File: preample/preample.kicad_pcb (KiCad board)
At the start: 4 copper layers, 158 x 37 mm, 74 parts, among them J1 Conn_01x03, J2 Conn_01x07, J3 Conn_01x06, SW1 SW_DPDT_x2, U1 TPS7A39, U2 OPA2134UA, U3 OPA134UA, U4 OPA2134UA, U5 OPA134UA

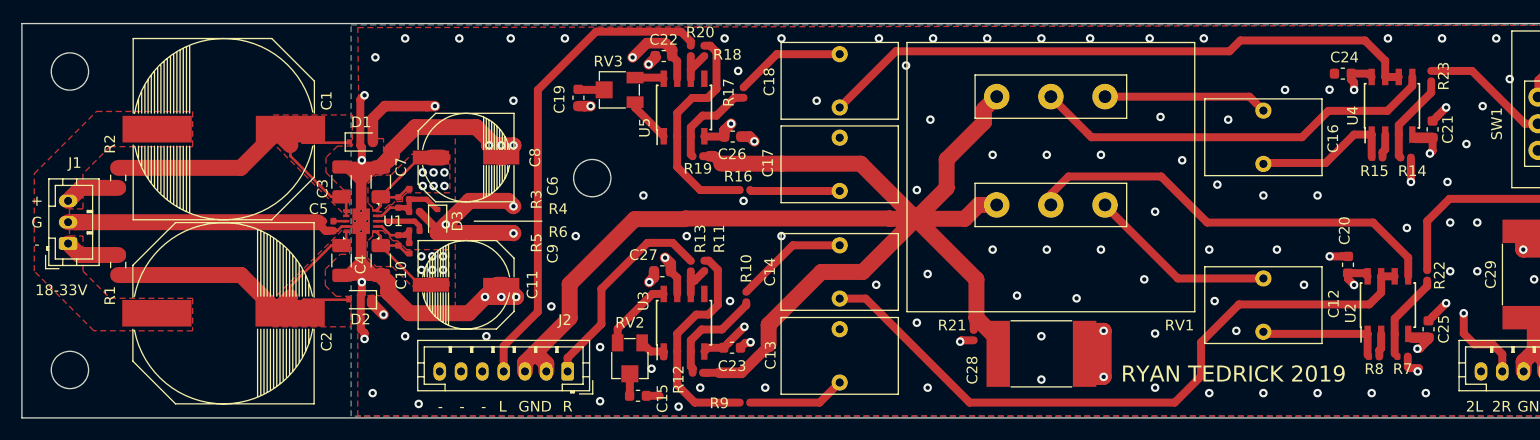
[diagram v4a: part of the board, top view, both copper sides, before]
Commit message: Changes resistors for opamps to 0805s. Chose more realistic power resistors. rerouted for new components.
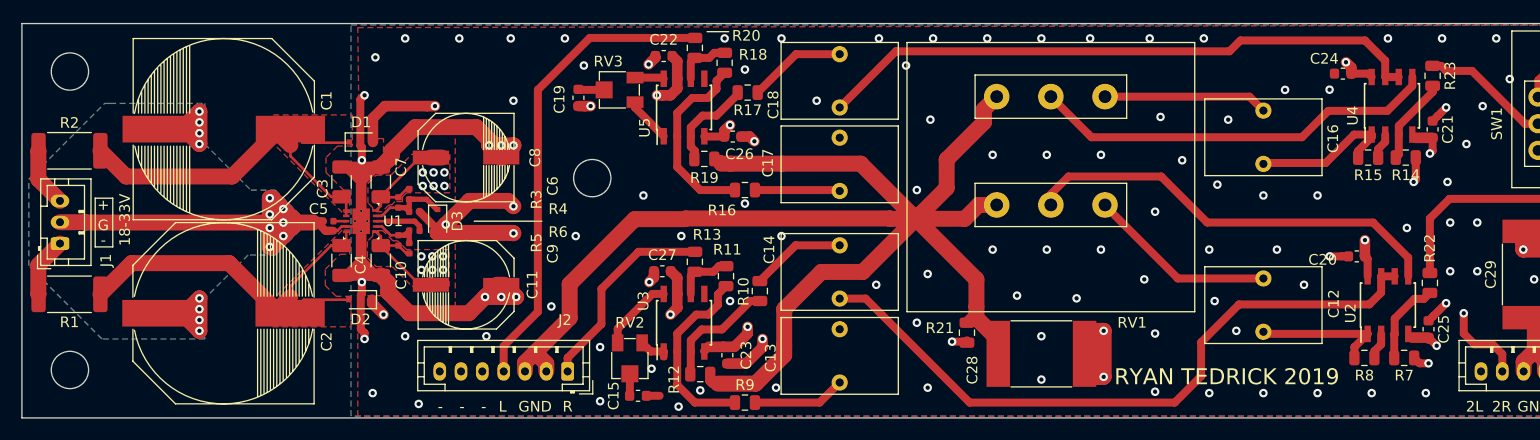
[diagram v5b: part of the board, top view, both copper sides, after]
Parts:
- R1, R2: value 3R -> 15R; footprint Resistor_SMD:R_0805_2012Metric -> Resistor_SMD:R_2512_6332Metric
- R10, R11, R12, R16, R17, R18, R19, R9: value 560R -> 5K6; footprint Resistor_SMD:R_0402_1005Metric -> Resistor_SMD:R_0805_2012Metric
- R13, R14, R15, R20, R21, R22, R23, R7, R8: footprint Resistor_SMD:R_0402_1005Metric -> Resistor_SMD:R_0805_2012Metric
- moved R1 5.33 mm to (50.5, 75.3), turned to 180 degrees
- moved R2 5.23 mm to (50.5, 61.8), turned to 0 degrees
- moved R11 2.25 mm to (112.1, 73.6), turned to 270 degrees
- moved R18 2.21 mm to (112.0, 53.6), turned to 270 degrees
- moved R10 1.39 mm to (115.3, 75.0)
- moved C20 1.14 mm to (171.3, 71.8), turned to 0 degrees
- moved R8 0.92 mm to (172.0, 81.3)
- moved R15 0.86 mm to (172.4, 62.5)
- moved C23 0.83 mm to (112.3, 81.0), turned to 90 degrees
- moved J1 0.76 mm to (49.7, 70.5)
- moved R22 0.76 mm to (178.2, 74.2)
- moved R21 0.67 mm to (134.7, 78.9)
- moved R19 0.66 mm to (110.1, 62.6)
- moved R13 0.56 mm to (109.2, 72.3)
- moved R20 0.47 mm to (109.2, 52.2)
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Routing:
- net GND: track 180.6 -> 222.1 mm, vias 120 -> 138
- net Net-(R16-Pad1): track 21.3 -> 17.8 mm
- net -24V: track 34.2 -> 37.5 mm
- net Net-(R11-Pad2): track 21.2 -> 17.9 mm
- net +24V: track 34.9 -> 37.9 mm
- net SIGNAL_GROUND: track 137.7 -> 140.1 mm
- net -15V: track 202.8 -> 201.0 mm
- net +15V: track 182.8 -> 181.1 mm
- net Net-(C14-Pad1): track 10.6 -> 8.88 mm
- net Net-(R11-Pad1): track 3.77 -> 5.37 mm
- net Net-(R10-Pad2): track 9.97 -> 11.2 mm
- net Net-(R18-Pad1): track 3.92 -> 5.10 mm
- net Net-(C18-Pad1): track 10.3 -> 9.19 mm
- net CH1_OUT: track 19.9 -> 19.3 mm
- net CH2_OUT: track 45.1 -> 44.5 mm
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- added copper zone on In2.Cu, net GND

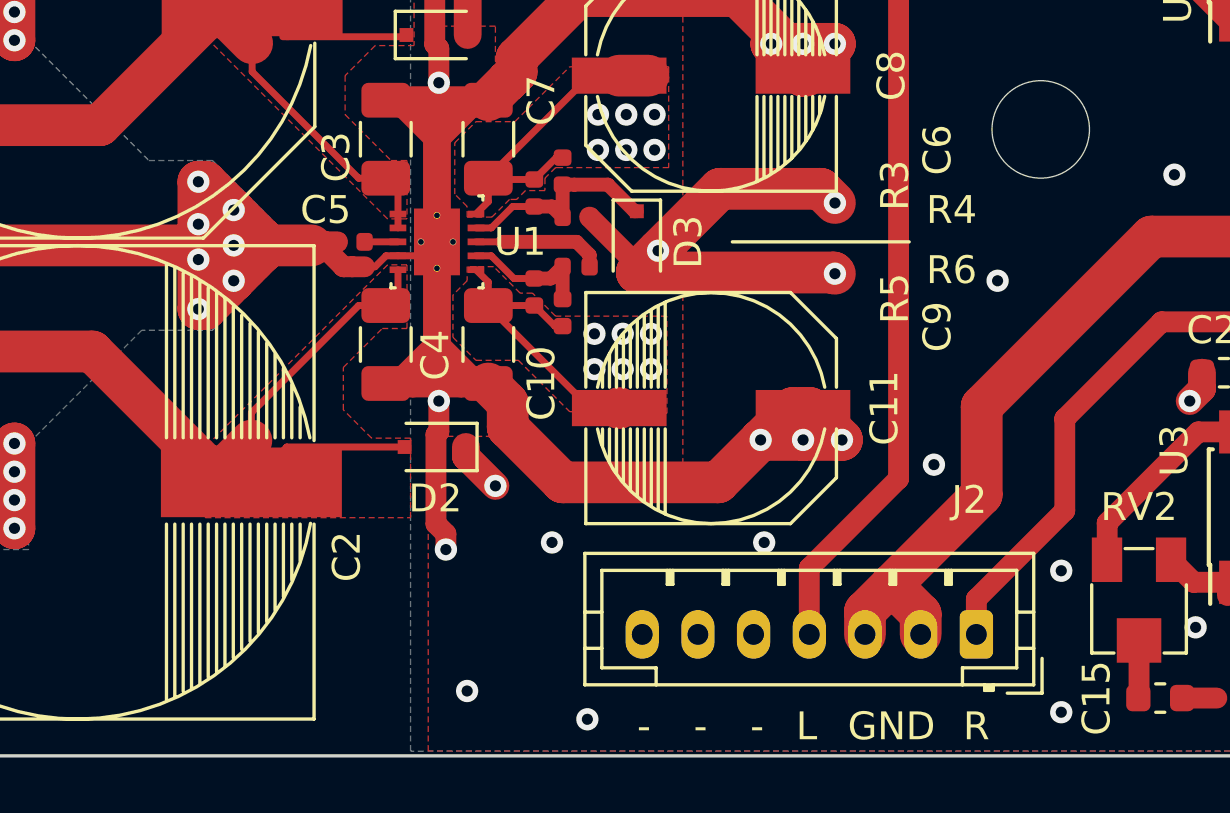
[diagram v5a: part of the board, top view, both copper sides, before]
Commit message: Added simulation. Added current path for negative feed forward cap. Chose resistors for amplifier circuits.
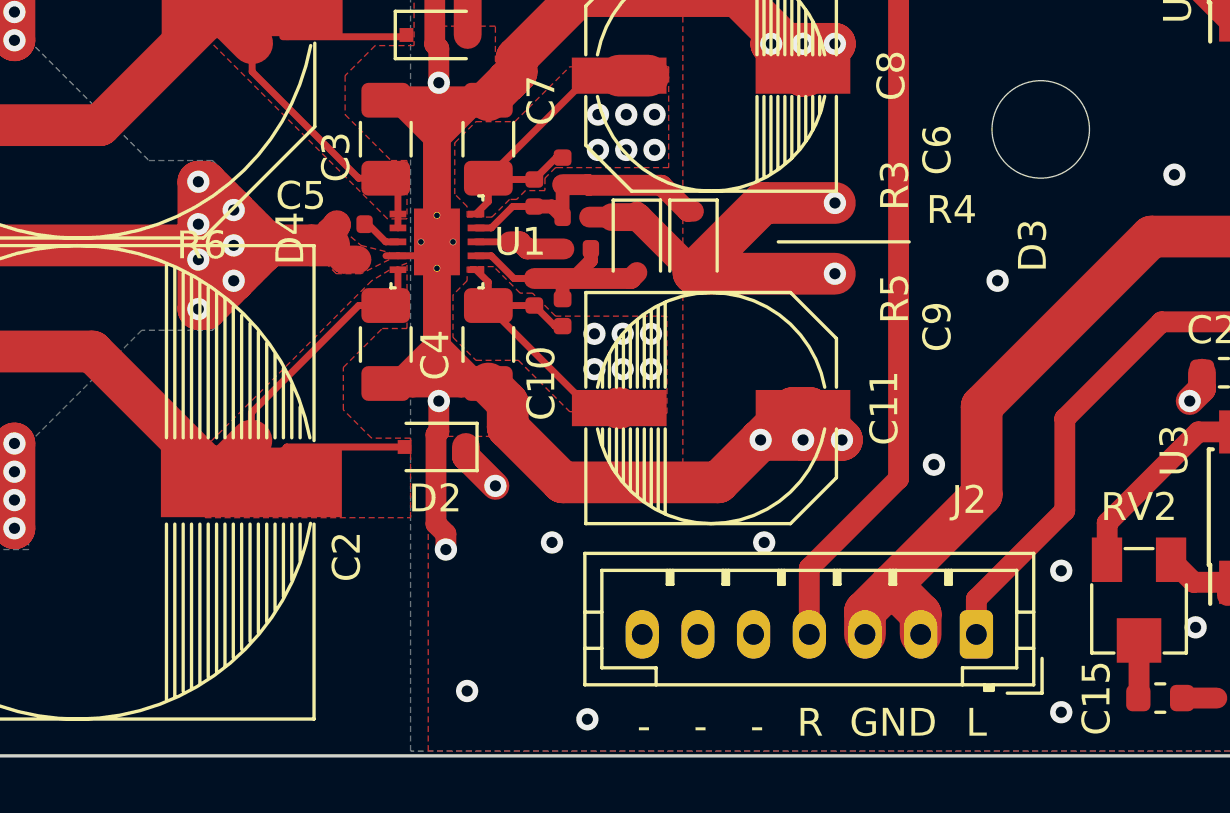
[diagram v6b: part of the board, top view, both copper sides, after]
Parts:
- added D4: D_Schottky_ALT, Diode_SMD:D_SOD-323F, F.Cu at (85.1, 68.5)
- R10, R11, R12, R16, R17, R18, R19, R9: value 5K6 -> 11K5
- moved D3 2.03 mm to (87.1, 68.5)
- moved R6 0.64 mm to (83.0, 68.7), turned to 0 degrees
- moved C5 0.64 mm to (74.8, 67.8)
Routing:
- net Net-(C9-Pad1): track 4.79 -> 9.75 mm
- net GND: track 222.1 -> 219.8 mm, vias 138 -> 137
- net Net-(C6-Pad2): track 7.82 -> 9.85 mm
- net Net-(R6-Pad1): track 4.70 -> 3.26 mm
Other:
- board text added: "CENTRAL MOUNTING HOLE: 49 MM RIGHT 18 MM UP FROM LOWER LEFT MOUNTING HOLE"
